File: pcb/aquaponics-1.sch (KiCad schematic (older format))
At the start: 17 parts, among them J1 5V Power Source, J2 Screw_Terminal_01x02, J3 Water Level Sensor, J4 Rain Sensor, J5 Conn_01x02_Female, M1 Growbed Pump, M2 Overflow Pump, M3 Fish Feeder, Q1 TIP120, Q2 TIP120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

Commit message: 1st draft
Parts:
- added R6: 10k, Resistor_THT:R_Axial_DIN0204_L3.6mm_D1.6mm_P5.08mm_Horizontal, symbol Device:R
- added U2: DHT11, Sensor:Aosong_DHT11_5.5x12.0_P2.54mm, symbol Sensor:DHT11
- J2: footprint TerminalBlock_Phoenix:TerminalBlock_Phoenix_MPT-0,5-2-2.54_1x02_P2.54mm_Horizontal -> TerminalBlock_Phoenix:TerminalBlock_Phoenix_PT-1,5-2-5.0-H_1x02_P5.00mm_Horizontal
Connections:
- net labels added: +1V5, +3.3V, +5V
- wire segments 72 -> 73
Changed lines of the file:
@@
-$EndComp
-$Comp
-L power:GND #PWR04
-U 1 1 61AA0671
-P 3350 2950
-F 0 "#PWR04" H 3350 2700 50  0001 C CNN
-F 1 "GND" V 3355 2822 50  0000 R CNN
-F 2 "" H 3350 2950 50  0001 C CNN
-F 3 "" H 3350 2950 50  0001 C CNN
-	1    3350 2950
-	0    1    1    0
 $EndComp
 $Comp
@@
 	1    0    0    -1
 $EndComp
-Wire Wire Line
-	3350 2950 3550 2950
 Wire Wire Line
 	3000 3050 3800 3050
@@
 Wire Wire Line
 	5900 2400 5400 2400
-Wire Wire Line
-	5400 2400 5400 3750
-Wire Wire Line
-	5400 3750 5000 3750
 Connection ~ 5900 2400
 Wire Wire Line
 	5900 2400 5900 2350
-Wire Wire Line
-	5050 2300 5050 2950
-Wire Wire Line
-	5050 2950 5000 2950
-Connection ~ 3550 2950
-Wire Wire Line
-	3550 2950 3800 2950
 Wire Wire Line
 	950  1100 1300 1100
@@
 Wire Wire Line
 	6100 3750 6300 3750
-Wire Wire Line
-	3800 3450 3600 3450
-Wire Wire Line
-	3600 3450 3600 4250
-Wire Wire Line
-	3600 4250 5750 4250
-Wire Wire Line
-	5750 4250 5750 3350
-Wire Wire Line
-	5750 3350 6300 3350
-Wire Wire Line
-	3800 3550 3650 3550
-Wire Wire Line
-	3650 3550 3650 4200
-Wire Wire Line
-	3650 4200 5650 4200
-Wire Wire Line
-	5650 4200 5650 3850
-Wire Wire Line
-	5650 3850 6300 3850
-Wire Wire Line
-	6300 3450 5500 3450
-Wire Wire Line
-	5500 3450 5500 3650
-Wire Wire Line
-	5500 3650 5000 3650
-Wire Wire Line
-	6300 3950 5250 3950
-Wire Wire Line
-	5250 3950 5250 3550
-Wire Wire Line
-	5250 3550 5000 3550
 $Comp
 L Connector:Screw_Terminal_01x02 J2
@@
 F 0 "J2" H 4830 1442 50  0000 L CNN
 F 1 "Screw_Terminal_01x02" H 4830 1351 50  0000 L CNN
-F 2 "TerminalBlock_Phoenix:TerminalBlock_Phoenix_MPT-0,5-2-2.54_1x02_P2.54mm_Horizontal" H 4750 1450 50  0001 C CNN
+F 2 "TerminalBlock_Phoenix:TerminalBlock_Phoenix_PT-1,5-2-5.0-H_1x02_P5.00mm_Horizontal" H 4750 1450 50  0001 C CNN
 F 3 "~" H 4750 1450 50  0001 C CNN
 	1    4750 1450
@@
 $EndComp
 Wire Wire Line
-	4200 1800 4100 1800
-Wire Wire Line
-	4100 1800 4100 2300
-Wire Wire Line
-	4100 2300 5050 2300
-Wire Wire Line
-	3550 1550 3550 2950
-Wire Wire Line
 	4550 850  4550 1300
 Wire Wire Line
@@
 Wire Wire Line
 	4550 1300 4550 1450
-Wire Wire Line
-	3550 1550 4550 1550
 $Comp
 L Device:R_PHOTO R1
@@
 $EndComp
 Wire Wire Line
-	5000 4050 5900 4050
-Wire Wire Line
-	5900 4050 5900 2900
-Wire Wire Line
 	950  1100 950  1750
 Connection ~ 950  1100
@@
 	950  2450 950  1750
 Connection ~ 950  1750
+$Comp
+L Sensor:DHT11 U2
+U 1 1 61B35334
+P 4400 5150
+F 0 "U2" H 4156 5196 50  0000 R CNN
+F 1 "DHT11" H 4156 5105 50  0000 R CNN
+F 2 "Sensor:Aosong_DHT11_5.5x12.0_P2.54mm" H 4400 4750 50  0001 C CNN
+F 3 "http://akizukidenshi.com/download/ds/aosong/DHT11.pdf" H 4550 5400 50  0001 C CNN
+	1    4400 5150
+	1    0    0    -1
+$EndComp
+$Comp
+L power:GND #PWR06
+U 1 1 61B37516
+P 4400 5550
+F 0 "#PWR06" H 4400 5300 50  0001 C CNN
+F 1 "GND" H 4405 5377 50  0000 C CNN
+F 2 "" H 4400 5550 50  0001 C CNN
+F 3 "" H 4400 5550 50  0001 C CNN
+	1    4400 5550
+	1    0    0    -1
+$EndComp
+Wire Wire Line
+	4400 5450 4400 5550
+$Comp
+L Device:R R6
+U 1 1 61B3D7D4
+P 4950 4650
+F 0 "R6" H 5020 4696 50  0000 L CNN
+F 1 "10k" H 5020 4605 50  0000 L CNN
+F 2 "Resistor_THT:R_Axial_DIN0204_L3.6mm_D1.6mm_P5.08mm_Horizontal" V 4880 4650 50  0001 C CNN
+F 3 "~" H 4950 4650 50  0001 C CNN
+	1    4950 4650
+	1    0    0    1
+$EndComp
+Wire Wire Line
+	5000 3450 5400 3450
+Wire Wire Line
+	5400 3450 5400 2400
+Wire Wire Line
+	6300 3550 6300 3450
+Wire Wire Line
+	5000 3550 6300 3550
+Wire Wire Line
+	6300 3950 5350 3950
+Wire Wire Line
+	5350 3950 5350 3650
+Wire Wire Line
+	5350 3650 5000 3650
+$Comp
+L power:+3.3V #PWR0103
+U 1 1 61B97206
+P 5100 3950
+F 0 "#PWR0103" H 5100 3800 50  0001 C CNN
+F 1 "+3.3V" V 5115 4078 50  0000 L CNN
+F 2 "" H 5100 3950 50  0001 C CNN
+F 3 "" H 5100 3950 50  0001 C CNN
+	1    5100 3950
+	0    1    1    0
+$EndComp
+Wire Wire Line
+	5100 3950 5000 3950
+Wire Wire Line
+	5000 3750 5550 3750
+Wire Wire Line
+	5550 3750 5550 5150
+Wire Wire Line
+	5550 5150 4950 5150
+$Comp
+L power:+3.3V #PWR0104
+U 1 1 61B9BD8B
+P 4400 4550
+F 0 "#PWR0104" H 4400 4400 50  0001 C CNN
+F 1 "+3.3V" H 4415 4723 50  0000 C CNN
+F 2 "" H 4400 4550 50  0001 C CNN
+F 3 "" H 4400 4550 50  0001 C CNN
+	1    4400 4550
+	1    0    0    -1
+$EndComp
+Wire Wire Line
+	4400 4550 4400 4600
+Wire Wire Line
+	4400 4600 4700 4600
+Wire Wire Line
+	4700 4600 4700 4500
+Wire Wire Line
+	4700 4500 4950 4500
+Connection ~ 4400 4600
+Wire Wire Line
+	4400 4600 4400 4850
+Wire Wire Line
+	4950 4800 4950 5150
+Connection ~ 4950 5150
+Wire Wire Line
+	4950 5150 4700 5150
+$Comp
+L power:+5V #PWR0105
+U 1 1 61BB705B
+P 5350 2950
+F 0 "#PWR0105" H 5350 2800 50  0001 C CNN
+F 1 "+5V" V 5365 3078 50  0000 L CNN
+F 2 "" H 5350 2950 50  0001 C CNN
+F 3 "" H 5350 2950 50  0001 C CNN
+	1    5350 2950
+	0    1    1    0
+$EndComp
+$Comp
+L power:+5V #PWR0106
+U 1 1 61BBB483
+P 3900 1800
+F 0 "#PWR0106" H 3900 1650 50  0001 C CNN
+F 1 "+5V" V 3915 1928 50  0000 L CNN
+F 2 "" H 3900 1800 50  0001 C CNN
+F 3 "" H 3900 1800 50  0001 C CNN
+	1    3900 1800
+	0    -1   -1   0
+$EndComp
+Wire Wire Line
+	3900 1800 4200 1800
+$Comp
+L power:+5V #PWR0107
+U 1 1 61BC0B4D
+P 5800 3400
+F 0 "#PWR0107" H 5800 3250 50  0001 C CNN
+F 1 "+5V" V 5815 3528 50  0000 L CNN
+F 2 "" H 5800 3400 50  0001 C CNN
+F 3 "" H 5800 3400 50  0001 C CNN
+	1    5800 3400
+	0    -1   -1   0
+$EndComp
+$Comp
+L power:+5V #PWR0108
+U 1 1 61BCA5A2
+P 5750 3850
+F 0 "#PWR0108" H 5750 3700 50  0001 C CNN
+F 1 "+5V" V 5765 3978 50  0000 L CNN
+F 2 "" H 5750 3850 50  0001 C CNN
+F 3 "" H 5750 3850 50  0001 C CNN
+	1    5750 3850
+	0    -1   -1   0
+$EndComp
+Wire Wire Line
+	5800 3400 6300 3400
+Wire Wire Line
+	6300 3400 6300 3350
+Wire Wire Line
+	5750 3850 6300 3850
+Wire Bus Line
+	7700 1650 7700 4000
+$Comp
+L power:+1V5 #PWR0109
+U 1 1 61BDFBA0
+P 7700 1350
+F 0 "#PWR0109" H 7700 1200 50  0001 C CNN
+F 1 "+1V5" H 7715 1523 50  0000 C CNN
+F 2 "" H 7700 1350 50  0001 C CNN
+F 3 "" H 7700 1350 50  0001 C CNN
+	1    7700 1350
+	1    0    0    -1
+$EndComp
+Wire Wire Line
+	7700 1650 7700 1350
+$Comp
+L power:+5V #PWR0110
+U 1 1 61C0E91D
+P 5900 3050
+F 0 "#PWR0110" H 5900 2900 50  0001 C CNN
+F 1 "+5V" H 5915 3223 50  0000 C CNN
+F 2 "" H 5900 3050 50  0001 C CNN
+F 3 "" H 5900 3050 50  0001 C CNN
+	1    5900 3050
+	-1   0    0    1
+$EndComp
+Wire Wire Line
+	5900 3050 5900 2900
+Wire Wire Line
+	5000 2950 5350 2950
+Wire Wire Line
+	3800 2950 3650 2950
+Wire Wire Line
+	4550 1550 3650 1550
+Wire Wire Line
+	3650 1550 3650 2950
+$Comp
+L power:GND #PWR?
+U 1 1 61C4FE01
+P 3650 1350
+F 0 "#PWR?" H 3650 1100 50  0001 C CNN
+F 1 "GND" H 3655 1177 50  0000 C CNN
+F 2 "" H 3650 1350 50  0001 C CNN
+F 3 "" H 3650 1350 50  0001 C CNN
+	1    3650 1350
+	-1   0    0    1
+$EndComp
+Wire Wire Line
+	3650 1350 3650 1550
+Connection ~ 3650 1550
 $EndSCHEMATC

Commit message: Update PCB'
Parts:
- J3, J4: footprint Connector_PinHeader_1.00mm:PinHeader_1x03_P1.00mm_Vertical -> Connector_PinHeader_2.54mm:PinHeader_1x03_P2.54mm_Vertical
- M1, M2, M3, R1: footprint Connector_PinHeader_1.00mm:PinHeader_1x02_P1.00mm_Vertical -> Connector_PinHeader_2.54mm:PinHeader_1x02_P2.54mm_Vertical
- R6: footprint Resistor_THT:R_Axial_DIN0204_L3.6mm_D1.6mm_P5.08mm_Horizontal -> Resistor_THT:R_Axial_DIN0204_L3.6mm_D1.6mm_P1.90mm_Vertical
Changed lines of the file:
@@
 F 0 "M1" H 1458 1296 50  0000 L CNN
 F 1 "Growbed Pump " H 1458 1205 50  0000 L CNN
-F 2 "Connector_PinHeader_1.00mm:PinHeader_1x02_P1.00mm_Vertical" H 1300 1210 50  0001 C CNN
+F 2 "Connector_PinHeader_2.54mm:PinHeader_1x02_P2.54mm_Vertical" H 1300 1210 50  0001 C CNN
 F 3 "~" H 1300 1210 50  0001 C CNN
 	1    1300 1300
@@
 F 0 "M2" H 1458 1946 50  0000 L CNN
 F 1 "Overflow Pump" H 1458 1855 50  0000 L CNN
-F 2 "Connector_PinHeader_1.00mm:PinHeader_1x02_P1.00mm_Vertical" H 1300 1860 50  0001 C CNN
+F 2 "Connector_PinHeader_2.54mm:PinHeader_1x02_P2.54mm_Vertical" H 1300 1860 50  0001 C CNN
 F 3 "~" H 1300 1860 50  0001 C CNN
 	1    1300 1950
@@
 F 0 "M3" H 1458 2646 50  0000 L CNN
 F 1 "Fish Feeder" H 1458 2555 50  0000 L CNN
-F 2 "Connector_PinHeader_1.00mm:PinHeader_1x02_P1.00mm_Vertical" H 1300 2560 50  0001 C CNN
+F 2 "Connector_PinHeader_2.54mm:PinHeader_1x02_P2.54mm_Vertical" H 1300 2560 50  0001 C CNN
 F 3 "~" H 1300 2560 50  0001 C CNN
 	1    1300 2650
@@
 F 0 "J3" H 6528 3376 50  0000 L CNN
 F 1 "Water Level Sensor" H 6528 3285 50  0000 L CNN
-F 2 "Connector_PinHeader_1.00mm:PinHeader_1x03_P1.00mm_Vertical" H 6500 3350 50  0001 C CNN
+F 2 "Connector_PinHeader_2.54mm:PinHeader_1x03_P2.54mm_Vertical" H 6500 3350 50  0001 C CNN
 F 3 "~" H 6500 3350 50  0001 C CNN
 	1    6500 3350
@@
 F 0 "J4" H 6528 3876 50  0000 L CNN
 F 1 "Rain Sensor" H 6528 3785 50  0000 L CNN
-F 2 "Connector_PinHeader_1.00mm:PinHeader_1x03_P1.00mm_Vertical" H 6500 3850 50  0001 C CNN
+F 2 "Connector_PinHeader_2.54mm:PinHeader_1x03_P2.54mm_Vertical" H 6500 3850 50  0001 C CNN
 F 3 "~" H 6500 3850 50  0001 C CNN
 	1    6500 3850
@@
 F 0 "R1" H 5970 2796 50  0000 L CNN
 F 1 "Light Sensor" H 5970 2705 50  0000 L CNN
-F 2 "Connector_PinHeader_1.00mm:PinHeader_1x02_P1.00mm_Vertical" V 5950 2500 50  0001 L CNN
+F 2 "Connector_PinHeader_2.54mm:PinHeader_1x02_P2.54mm_Vertical" V 5950 2500 50  0001 L CNN
 F 3 "~" H 5900 2700 50  0001 C CNN
 	1    5900 2750
@@
 F 0 "R6" H 5020 4696 50  0000 L CNN
 F 1 "10k" H 5020 4605 50  0000 L CNN
-F 2 "Resistor_THT:R_Axial_DIN0204_L3.6mm_D1.6mm_P5.08mm_Horizontal" V 4880 4650 50  0001 C CNN
+F 2 "Resistor_THT:R_Axial_DIN0204_L3.6mm_D1.6mm_P1.90mm_Vertical" V 4880 4650 50  0001 C CNN
 F 3 "~" H 4950 4650 50  0001 C CNN
 	1    4950 4650
@@
 L power:+5V #PWR0105
 U 1 1 61BB705B
-P 5350 2950
-F 0 "#PWR0105" H 5350 2800 50  0001 C CNN
-F 1 "+5V" V 5365 3078 50  0000 L CNN
-F 2 "" H 5350 2950 50  0001 C CNN
-F 3 "" H 5350 2950 50  0001 C CNN
-	1    5350 2950
+P 5200 2950
+F 0 "#PWR0105" H 5200 2800 50  0001 C CNN
+F 1 "+5V" V 5215 3078 50  0000 L CNN
+F 2 "" H 5200 2950 50  0001 C CNN
+F 3 "" H 5200 2950 50  0001 C CNN
+	1    5200 2950
 	0    1    1    0
 $EndComp
@@
 	5900 3050 5900 2900
 Wire Wire Line
-	5000 2950 5350 2950
-Wire Wire Line
 	3800 2950 3650 2950
 Wire Wire Line
@@
 	3650 1550 3650 2950
 $Comp
-L power:GND #PWR?
+L power:GND #PWR0111
 U 1 1 61C4FE01
 P 3650 1350
-F 0 "#PWR?" H 3650 1100 50  0001 C CNN
+F 0 "#PWR0111" H 3650 1100 50  0001 C CNN
 F 1 "GND" H 3655 1177 50  0000 C CNN
 F 2 "" H 3650 1350 50  0001 C CNN
@@
 	3650 1350 3650 1550
 Connection ~ 3650 1550
+Wire Wire Line
+	5000 2950 5200 2950
 $EndSCHEMATC

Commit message: Update PCB /
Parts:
- added D1: DIODE, Diode_THT:D_DO-15_P2.54mm_Vertical_AnodeUp, symbol pspice:DIODE
- R3: value 330 -> 10k
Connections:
- net labels removed: +1V5
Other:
- moved on the sheet: J2
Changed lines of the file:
@@
 P 5900 2200
 F 0 "R3" H 5970 2246 50  0000 L CNN
-F 1 "330" H 5970 2155 50  0000 L CNN
+F 1 "10k" H 5970 2155 50  0000 L CNN
 F 2 "Resistor_THT:R_Axial_DIN0204_L3.6mm_D1.6mm_P1.90mm_Vertical" V 5830 2200 50  0001 C CNN
 F 3 "~" H 5900 2200 50  0001 C CNN
@@
 Wire Wire Line
 	950  1100 950  850
-Wire Wire Line
-	950  850  4550 850
 $Comp
 L Connector:Conn_01x02_Female J1
@@
 L Connector:Screw_Terminal_01x02 J2
 U 1 1 61B3F470
-P 4750 1450
-F 0 "J2" H 4830 1442 50  0000 L CNN
-F 1 "Screw_Terminal_01x02" H 4830 1351 50  0000 L CNN
-F 2 "TerminalBlock_Phoenix:TerminalBlock_Phoenix_PT-1,5-2-5.0-H_1x02_P5.00mm_Horizontal" H 4750 1450 50  0001 C CNN
-F 3 "~" H 4750 1450 50  0001 C CNN
-	1    4750 1450
+P 5200 1300
+F 0 "J2" H 5280 1292 50  0000 L CNN
+F 1 "Screw_Terminal_01x02" H 5280 1201 50  0000 L CNN
+F 2 "TerminalBlock_Phoenix:TerminalBlock_Phoenix_PT-1,5-2-5.0-H_1x02_P5.00mm_Horizontal" H 5200 1300 50  0001 C CNN
+F 3 "~" H 5200 1300 50  0001 C CNN
+	1    5200 1300
 	1    0    0    -1
 $EndComp
@@
 Connection ~ 4550 1300
 Wire Wire Line
-	4550 1300 4550 1450
+	4550 1300 5000 1300
 $Comp
 L Device:R_PHOTO R1
@@
 	5100 3950 5000 3950
 Wire Wire Line
-	5000 3750 5550 3750
-Wire Wire Line
-	5550 3750 5550 5150
-Wire Wire Line
 	5550 5150 4950 5150
 $Comp
@@
 Wire Wire Line
 	5750 3850 6300 3850
-Wire Bus Line
-	7700 1650 7700 4000
-$Comp
-L power:+1V5 #PWR0109
-U 1 1 61BDFBA0
-P 7700 1350
-F 0 "#PWR0109" H 7700 1200 50  0001 C CNN
-F 1 "+1V5" H 7715 1523 50  0000 C CNN
-F 2 "" H 7700 1350 50  0001 C CNN
-F 3 "" H 7700 1350 50  0001 C CNN
-	1    7700 1350
-	1    0    0    -1
-$EndComp
-Wire Wire Line
-	7700 1650 7700 1350
 $Comp
 L power:+5V #PWR0110
@@
 Wire Wire Line
 	3800 2950 3650 2950
-Wire Wire Line
-	4550 1550 3650 1550
-Wire Wire Line
-	3650 1550 3650 2950
 $Comp
 L power:GND #PWR0111
@@
 $EndComp
 Wire Wire Line
-	3650 1350 3650 1550
-Connection ~ 3650 1550
-Wire Wire Line
 	5000 2950 5200 2950
+Wire Wire Line
+	5550 5150 5550 4050
+Wire Wire Line
+	5550 4050 5000 4050
+$Comp
+L pspice:DIODE D1
+U 1 1 61C3F641
+P 4100 1400
+F 0 "D1" H 4100 1135 50  0000 C CNN
+F 1 "DIODE" H 4100 1226 50  0000 C CNN
+F 2 "Diode_THT:D_DO-15_P2.54mm_Vertical_AnodeUp" H 4100 1400 50  0001 C CNN
+F 3 "~" H 4100 1400 50  0001 C CNN
+	1    4100 1400
+	-1   0    0    1
+$EndComp
+Wire Wire Line
+	950  850  4550 850
+Wire Wire Line
+	3650 1350 3650 1400
+Wire Wire Line
+	5000 1400 4300 1400
+Wire Wire Line
+	3900 1400 3650 1400
+Connection ~ 3650 1400
+Wire Wire Line
+	3650 1400 3650 2950
 $EndSCHEMATC

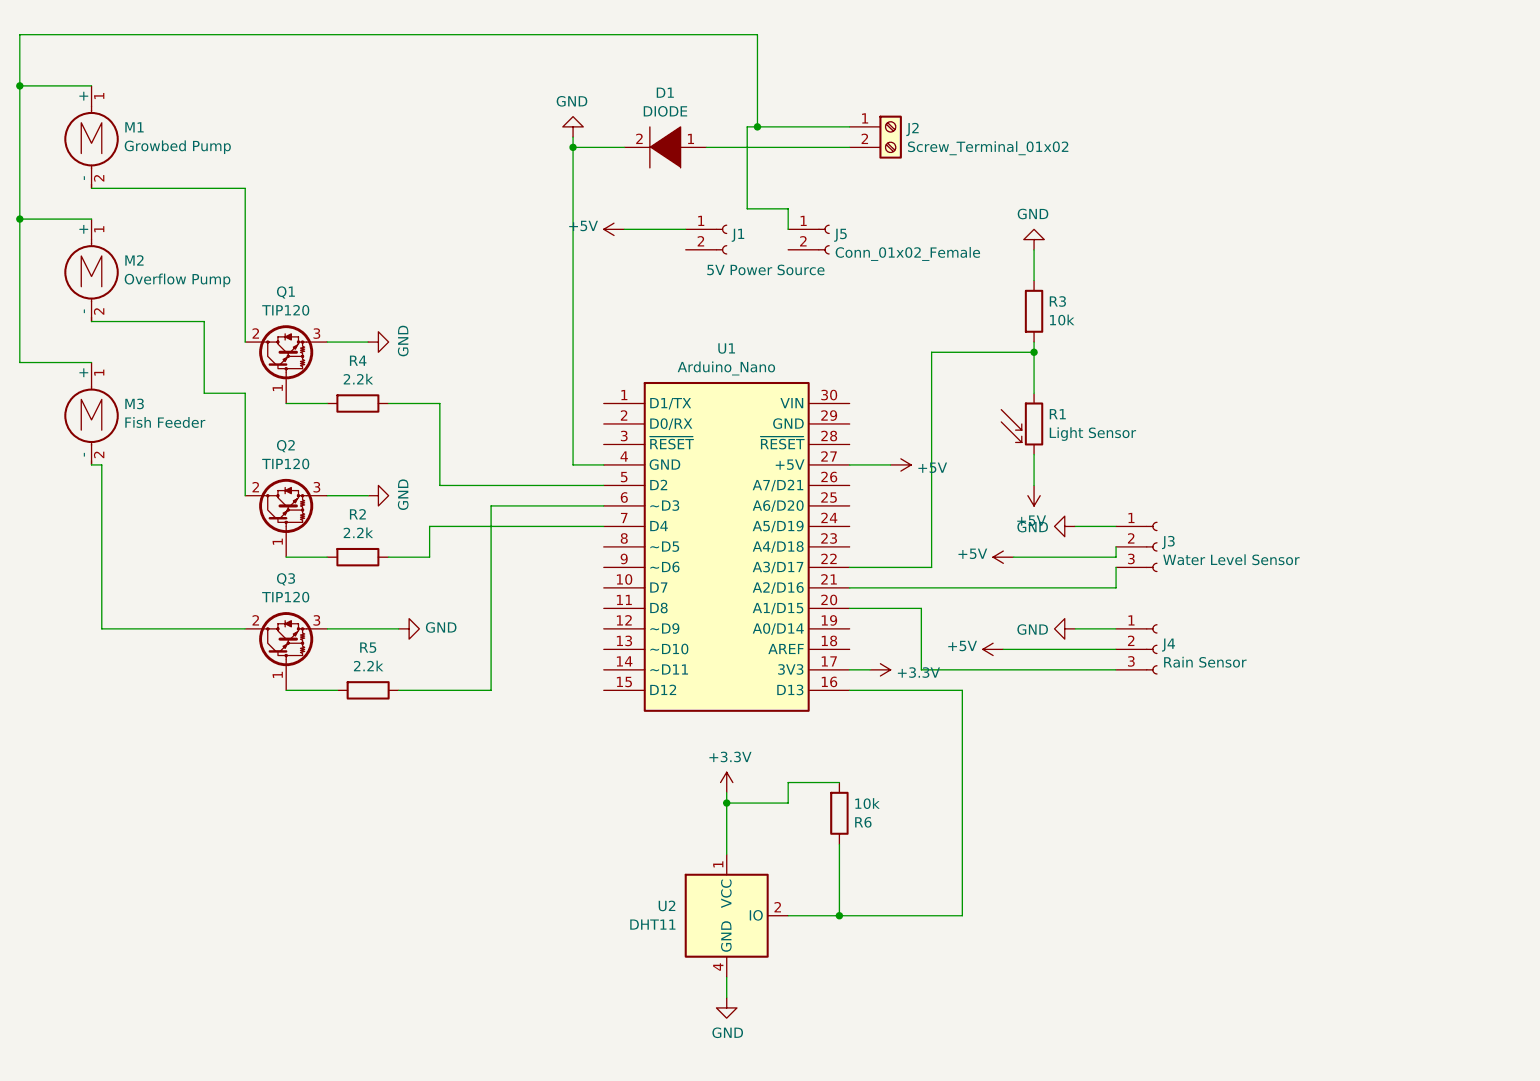
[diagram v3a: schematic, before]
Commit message: Changes after initial circuit print
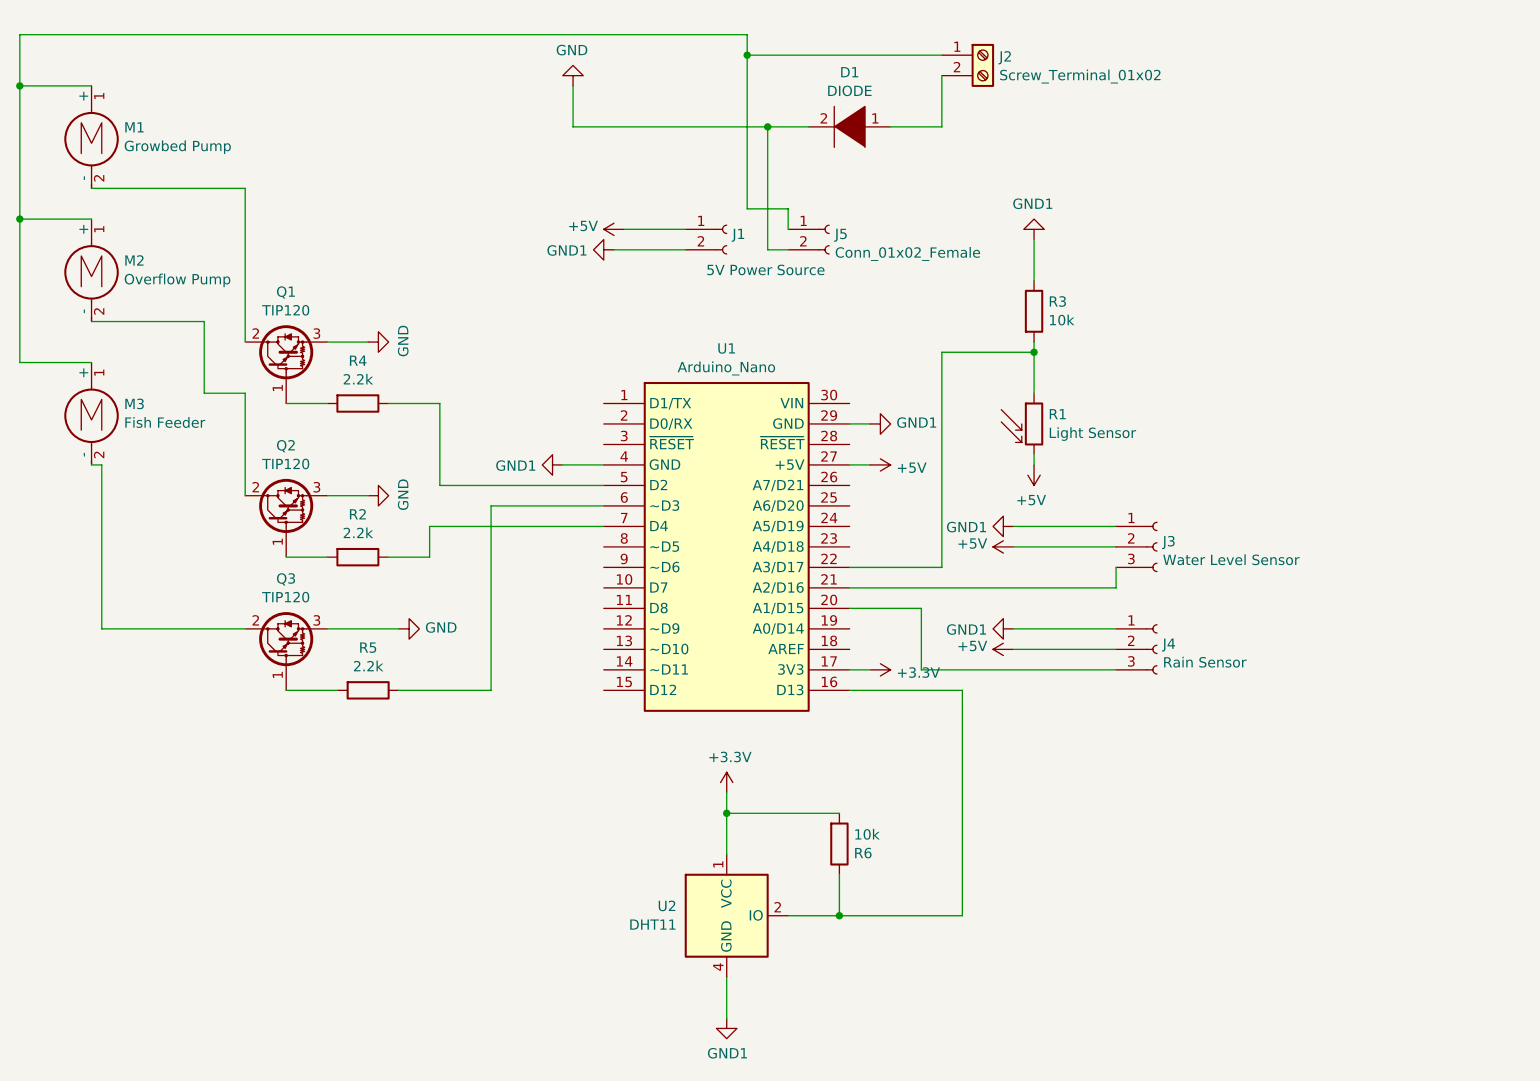
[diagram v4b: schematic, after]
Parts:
- J1, J5: footprint Connector_TE-Connectivity:TE_826576-2_1x02_P3.96mm_Vertical -> aquaponics-1:VP-TE_826576-2_1x02_P3.96mm_Vertical
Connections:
- net GND: now also J5.2 (Pin_2); no longer J3.1 (Pin_1), J4.1 (Pin_1), R3.1, U1.4 (GND), U2.4 (GND)
- net GND1: now reaches U1.29 (GND)
- net GND1: now also J1.2 (Pin_2), J3.1 (Pin_1), J4.1 (Pin_1), R3.1, U1.4 (GND), U2.4 (GND)
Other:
- moved on the sheet: D1, J2, R6
